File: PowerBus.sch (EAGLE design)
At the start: 14 parts, among them X1 5566-2, X10 5566-4, X11 5566-4, X12 5566-4, X13 5566-4, X2 5566-2, X3 5566-2, X4 5566-2, X5 5566-2, X6 5566-4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

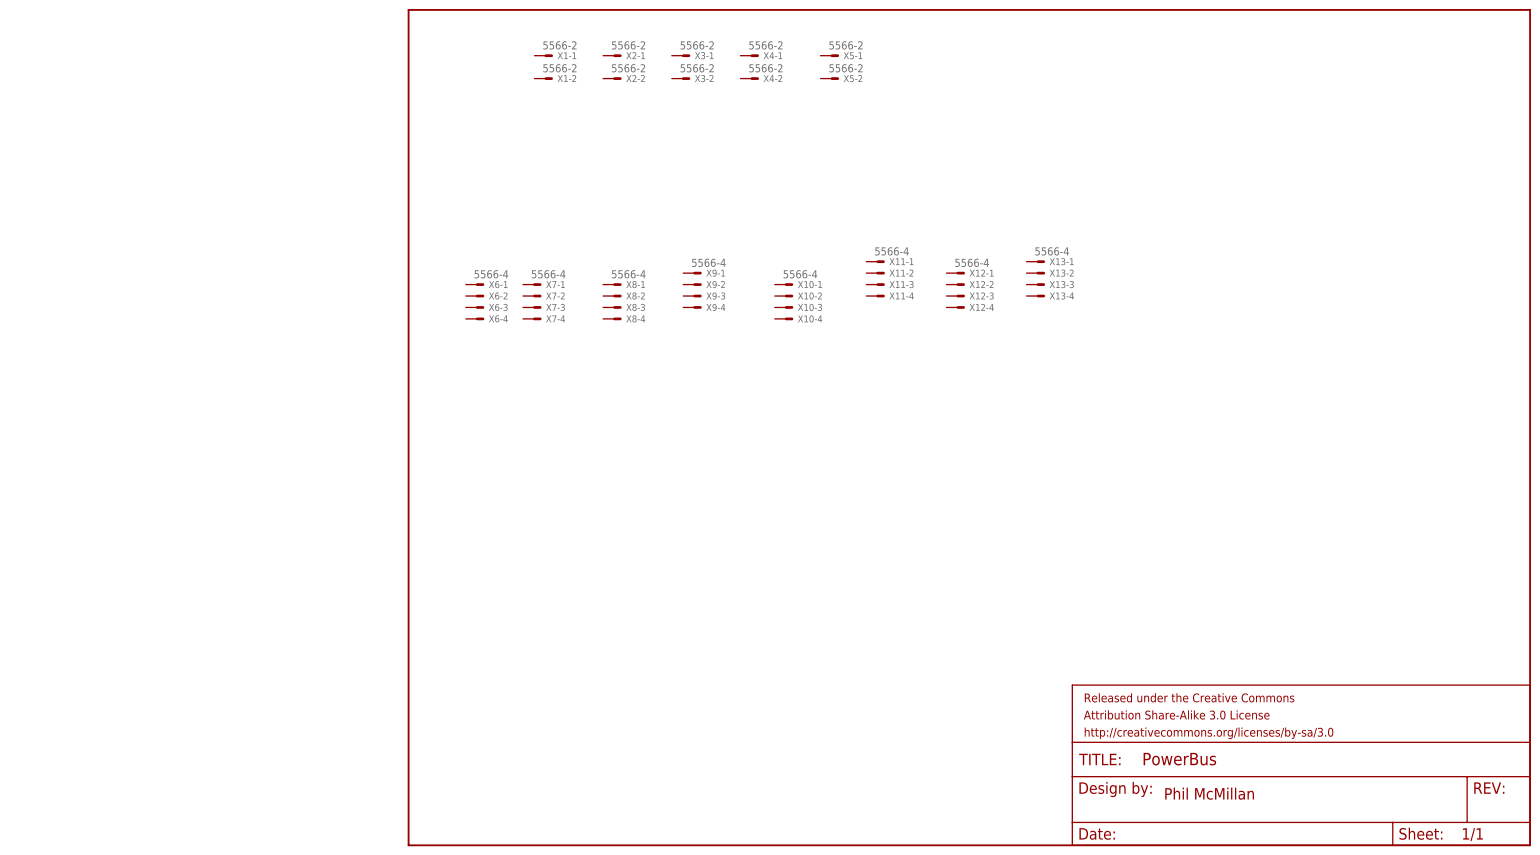
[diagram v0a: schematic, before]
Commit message: PM - Updated schematic; created board layout
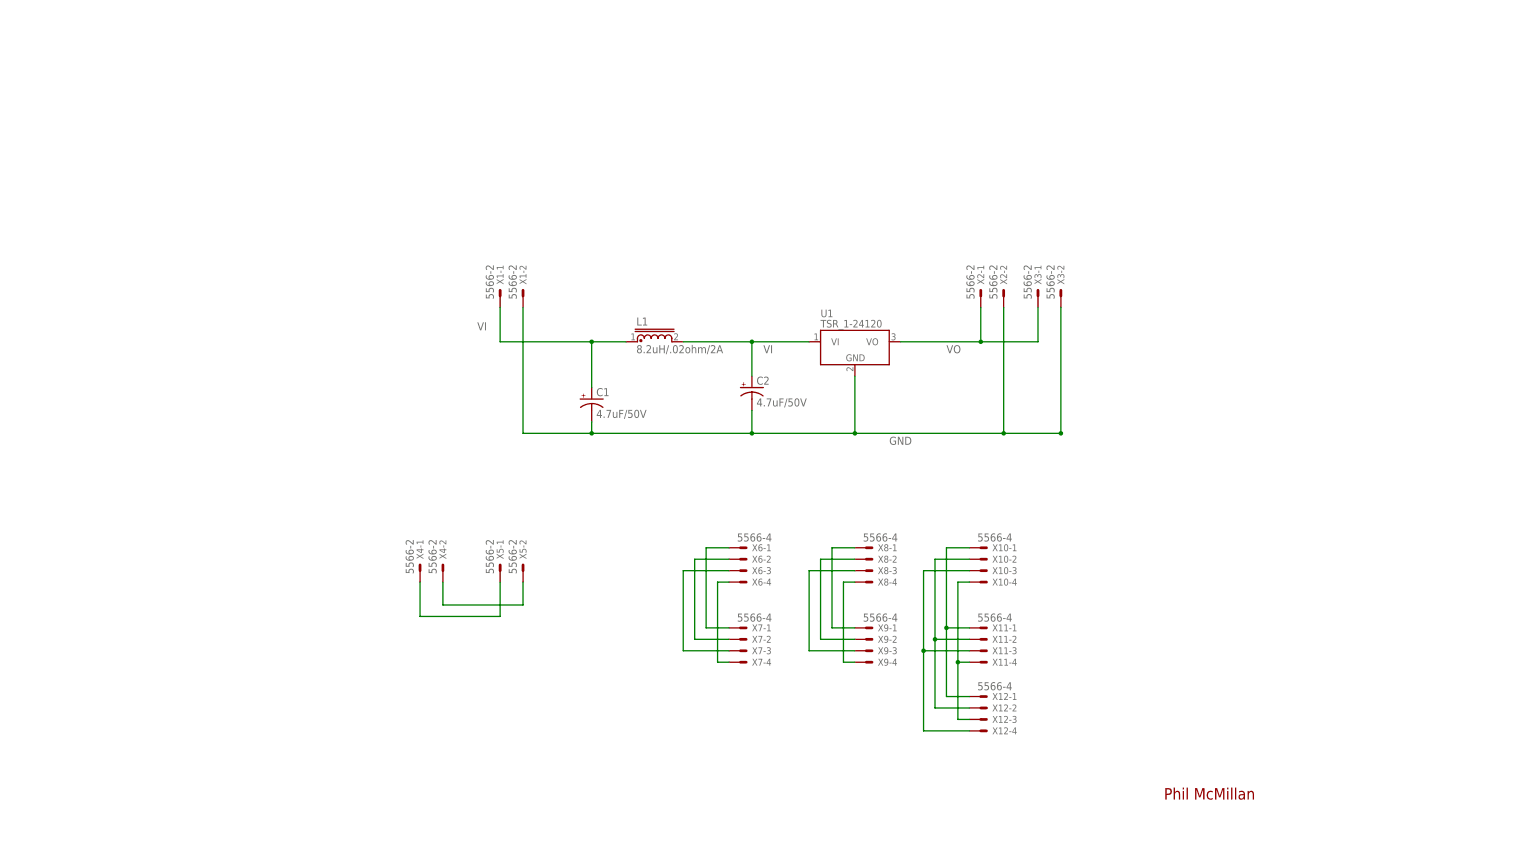
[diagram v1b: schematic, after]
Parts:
- removed FRAME1: FRAME-LETTER, SparkFun-Aesthetics:FRAME-LETTER
- removed X13: 5566-4, con-molex:5566-4
- added C1, C2: 4.7uF/50V, rcl:CPOL-USE2-5
- added L1: 8.2uH/.02ohm/2A, inductor-multicomp:MCAP103722016A-8R2MU
- added U1: TSR_1-24120, _traco_tsr-1:TSR_1-24120
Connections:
- new net GND: C1.-, C2.-, U1.GND, X1-2.S, X2-2.S, X3-2.S
- new net N$1: X6-1.S, X7-1.S
- new net N$10: X8-4.S, X9-4.S
- new net N$11: X10-1.S, X11-1.S, X12-1.S
- new net N$12: X10-2.S, X11-2.S, X12-2.S
- new net N$13: X10-3.S, X11-3.S, X12-4.S
- new net N$14: X10-4.S, X11-4.S, X12-3.S
- new net N$2: X6-2.S, X7-2.S
- new net N$3: X6-3.S, X7-3.S
- new net N$4: X6-4.S, X7-4.S
- new net N$5: X4-1.S, X5-1.S
- new net N$6: X4-2.S, X5-2.S
- new net N$7: X8-1.S, X9-1.S
- new net N$8: X8-2.S, X9-2.S
- new net N$9: X8-3.S, X9-3.S
- new net VI: C1.+, C2.+, L1.1, L1.2, U1.VI, X1-1.S
- new net VO: U1.VO, X2-1.S, X3-1.S
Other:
- moved on the sheet: X1-1, X1-2, X10-1, X10-2, X10-3, X10-4, X11-1, X11-2, X11-3, X11-4, X12-1, X12-2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

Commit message: PM - Updated schematic and board. Initial prototype from OSHPark
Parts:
- added C3, C4: 4.7uF/50V, rcl:CPOL-USE2-5
- added JP1, JP2: (no value), pinhead:PINHD-1X10
- added JP3, JP4: (no value), pinhead:PINHD-1X8
- added JP7, JP8: (no value), pinhead:PINHD-1X6
- added L2: 8.2uH/.02ohm/2A, inductor-multicomp:MCAP103722016A-8R2MU
- added U2: TSR_1-2490, _traco_tsr-1:TSR_1-2490
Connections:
- new net N$15: JP1.3, JP2.3
- new net N$16: JP1.5, JP2.5
- new net N$17: JP1.6, JP2.6
- new net N$18: JP1.7, JP2.7
- new net N$19: JP1.8, JP2.8
- new net N$20: JP1.9, JP2.9
- new net N$21: JP1.10, JP2.10
- new net N$22: JP1.4, JP2.4
- new net N$24: JP3.1, JP4.1
- new net N$25: JP3.2, JP4.2
- new net N$26: JP3.3, JP4.3
- new net N$27: JP3.4, JP4.4
- new net N$28: JP3.5, JP4.5
- new net N$29: JP3.6, JP4.6
- new net N$30: JP3.7, JP4.7
- new net N$31: JP3.8, JP4.8
- new net N$39: JP7.1, JP8.1
- new net N$40: JP7.2, JP8.2
- new net N$41: JP7.3, JP8.3
- new net N$42: JP7.4, JP8.4
- new net N$43: JP7.5, JP8.5
- new net N$44: JP7.6, JP8.6
- new net VI2: C2.+, L1.2, U1.VI
- new net VI3: C4.+, L2.2, U2.VI
- new net VO2: U2.VO, X4-1.S, X5-1.S
- net GND: now also C3.-, C4.-, U2.GND, X4-2.S, X5-2.S
- net N$5: now also JP1.1, JP2.1; no longer X4-1.S, X5-1.S
- net N$6: now also JP1.2, JP2.2; no longer X4-2.S, X5-2.S
- net VI: now also C3.+, L2.1; no longer C2.+, L1.2, U1.VI
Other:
- moved on the sheet: C1, X1-1, X1-2, X4-1, X4-2, X5-1, X5-2
